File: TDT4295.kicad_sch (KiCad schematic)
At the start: 0 parts

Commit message: MCU SD-card merge
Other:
- added sheet MCU (MCU.kicad_sch)
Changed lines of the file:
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@@
+	)
+	(sheet
+		(at 140.97 15.24)
+		(size 48.26 38.1)
+		(exclude_from_sim no)
+		(in_bom yes)
+		(on_board yes)
+		(dnp no)
+		(fields_autoplaced yes)
+		(stroke
+			(width 0.1524)
+			(type solid)
+		)
+		(fill
+			(color 0 0 0 0.0000)
+		)
+		(property "Sheetname" "MCU"
+			(at 140.97 14.5284 0)
+			(effects
+				(font
+					(size 1.27 1.27)
+				)
+				(justify left bottom)
+			)
+		)
+		(property "Sheetfile" "MCU.kicad_sch"
+			(at 140.97 53.9246 0)
+			(effects
+				(font
+					(size 1.27 1.27)
+				)
+				(justify left top)
+			)
+		)
+		(instances
+			(project "TDT4295"
+				(path "/071102f3-276b-4b6b-8738-8c534a30b197"
+					(page "4")
+				)
+			)
+		)
 	)
 	(sheet

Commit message: link fpga
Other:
- added sheet FPGA (FPGA.kicad_sch)
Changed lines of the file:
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@@
+	)
+	(sheet
+		(at 19.05 45.72)
+		(size 38.735 33.02)
+		(exclude_from_sim no)
+		(in_bom yes)
+		(on_board yes)
+		(dnp no)
+		(fields_autoplaced yes)
+		(stroke
+			(width 0.1524)
+			(type solid)
+		)
+		(fill
+			(color 0 0 0 0.0000)
+		)
+		(property "Sheetname" "FPGA"
+			(at 19.05 45.0084 0)
+			(effects
+				(font
+					(size 1.27 1.27)
+				)
+				(justify left bottom)
+			)
+		)
+		(property "Sheetfile" "FPGA.kicad_sch"
+			(at 19.05 79.3246 0)
+			(effects
+				(font
+					(size 1.27 1.27)
+				)
+				(justify left top)
+			)
+		)
+		(instances
+			(project "TDT4295"
+				(path "/071102f3-276b-4b6b-8738-8c534a30b197"
+					(page "6")
+				)
+			)
+		)
 	)
 	(sheet

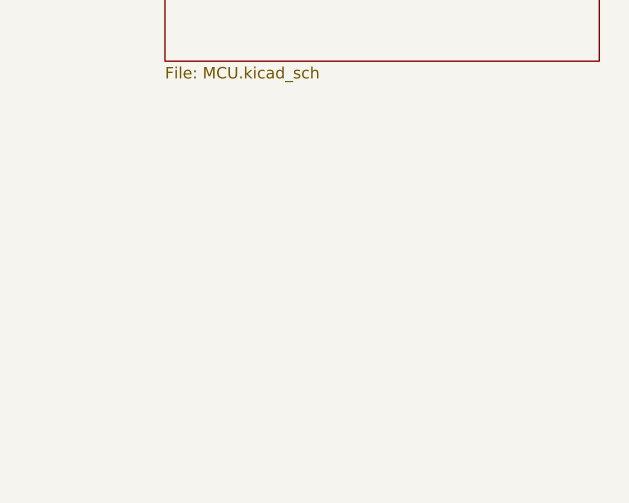
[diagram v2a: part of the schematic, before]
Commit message: schematic for stm32u545
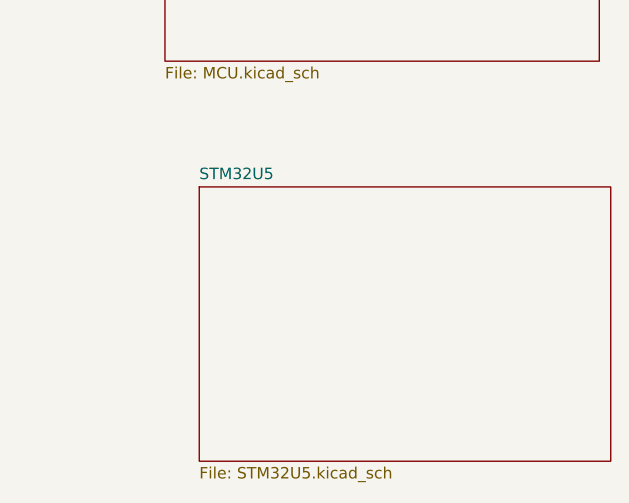
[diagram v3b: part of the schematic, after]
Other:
- added sheet STM32U5 (STM32U5.kicad_sch)
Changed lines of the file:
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@@
+	)
+	(sheet
+		(at 144.78 67.31)
+		(size 45.72 30.48)
+		(exclude_from_sim no)
+		(in_bom yes)
+		(on_board yes)
+		(dnp no)
+		(fields_autoplaced yes)
+		(stroke
+			(width 0.1524)
+			(type solid)
+		)
+		(fill
+			(color 0 0 0 0.0000)
+		)
+		(property "Sheetname" "STM32U5"
+			(at 144.78 66.5984 0)
+			(effects
+				(font
+					(size 1.27 1.27)
+				)
+				(justify left bottom)
+			)
+		)
+		(property "Sheetfile" "STM32U5.kicad_sch"
+			(at 144.78 98.3746 0)
+			(effects
+				(font
+					(size 1.27 1.27)
+				)
+				(justify left top)
+			)
+		)
+		(instances
+			(project "TDT4295"
+				(path "/071102f3-276b-4b6b-8738-8c534a30b197"
+					(page "7")
+				)
+			)
+		)
 	)
 	(sheet

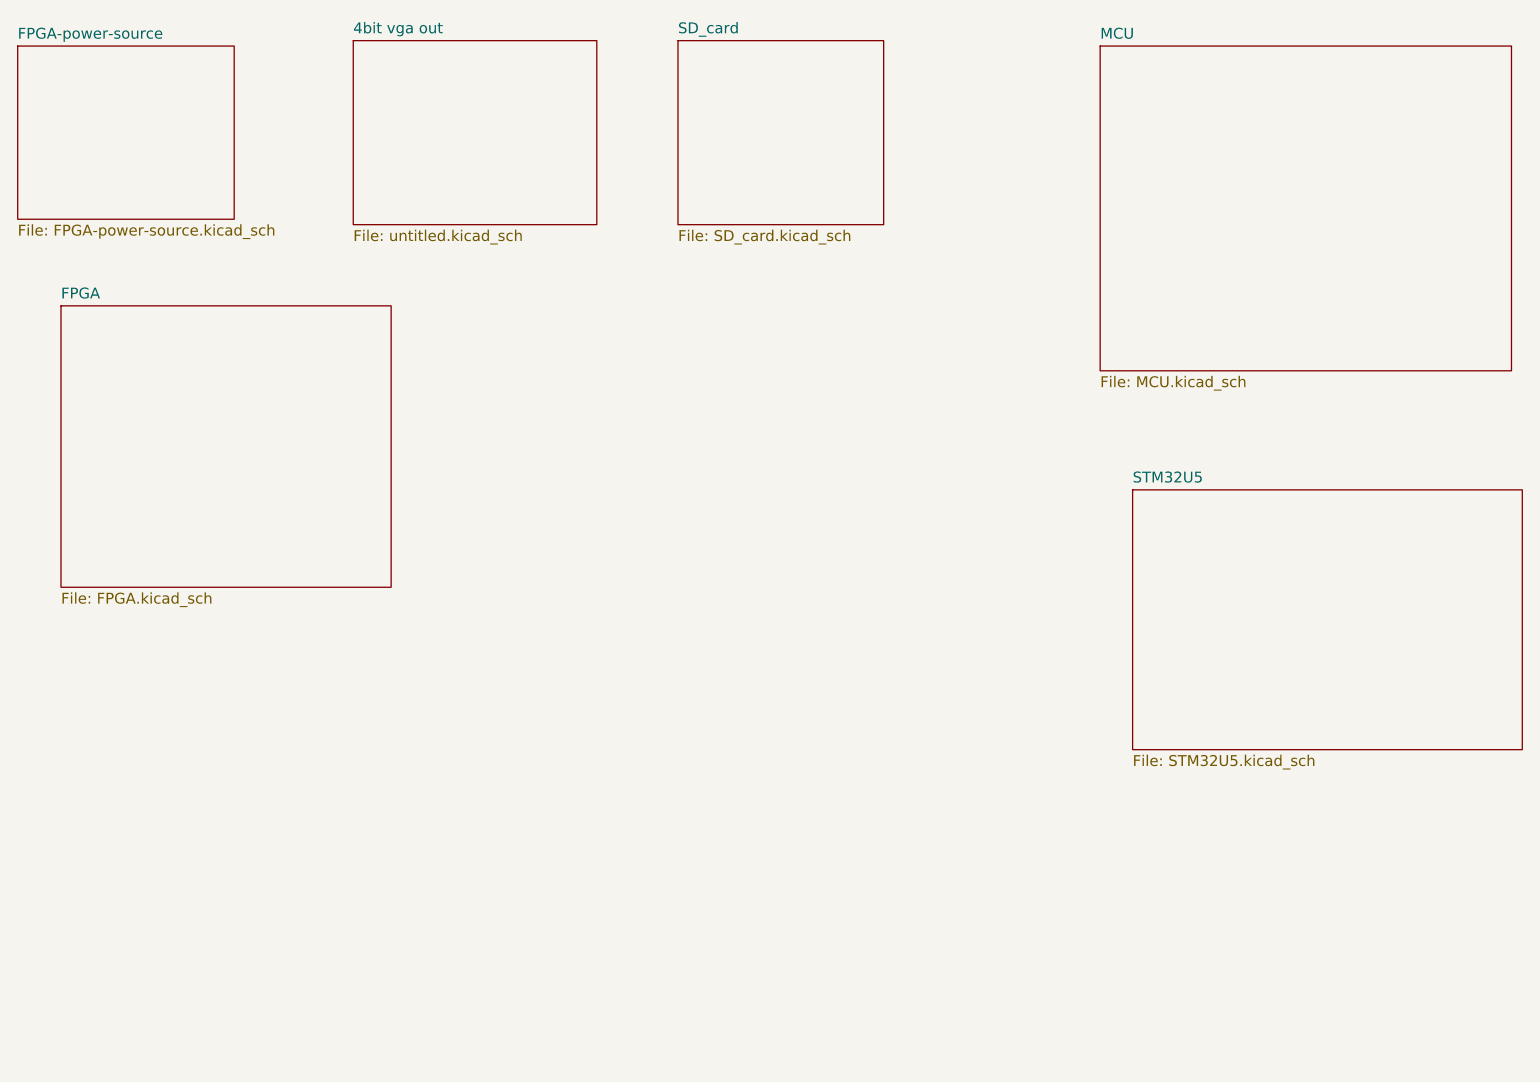
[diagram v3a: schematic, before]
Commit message: Added controllers
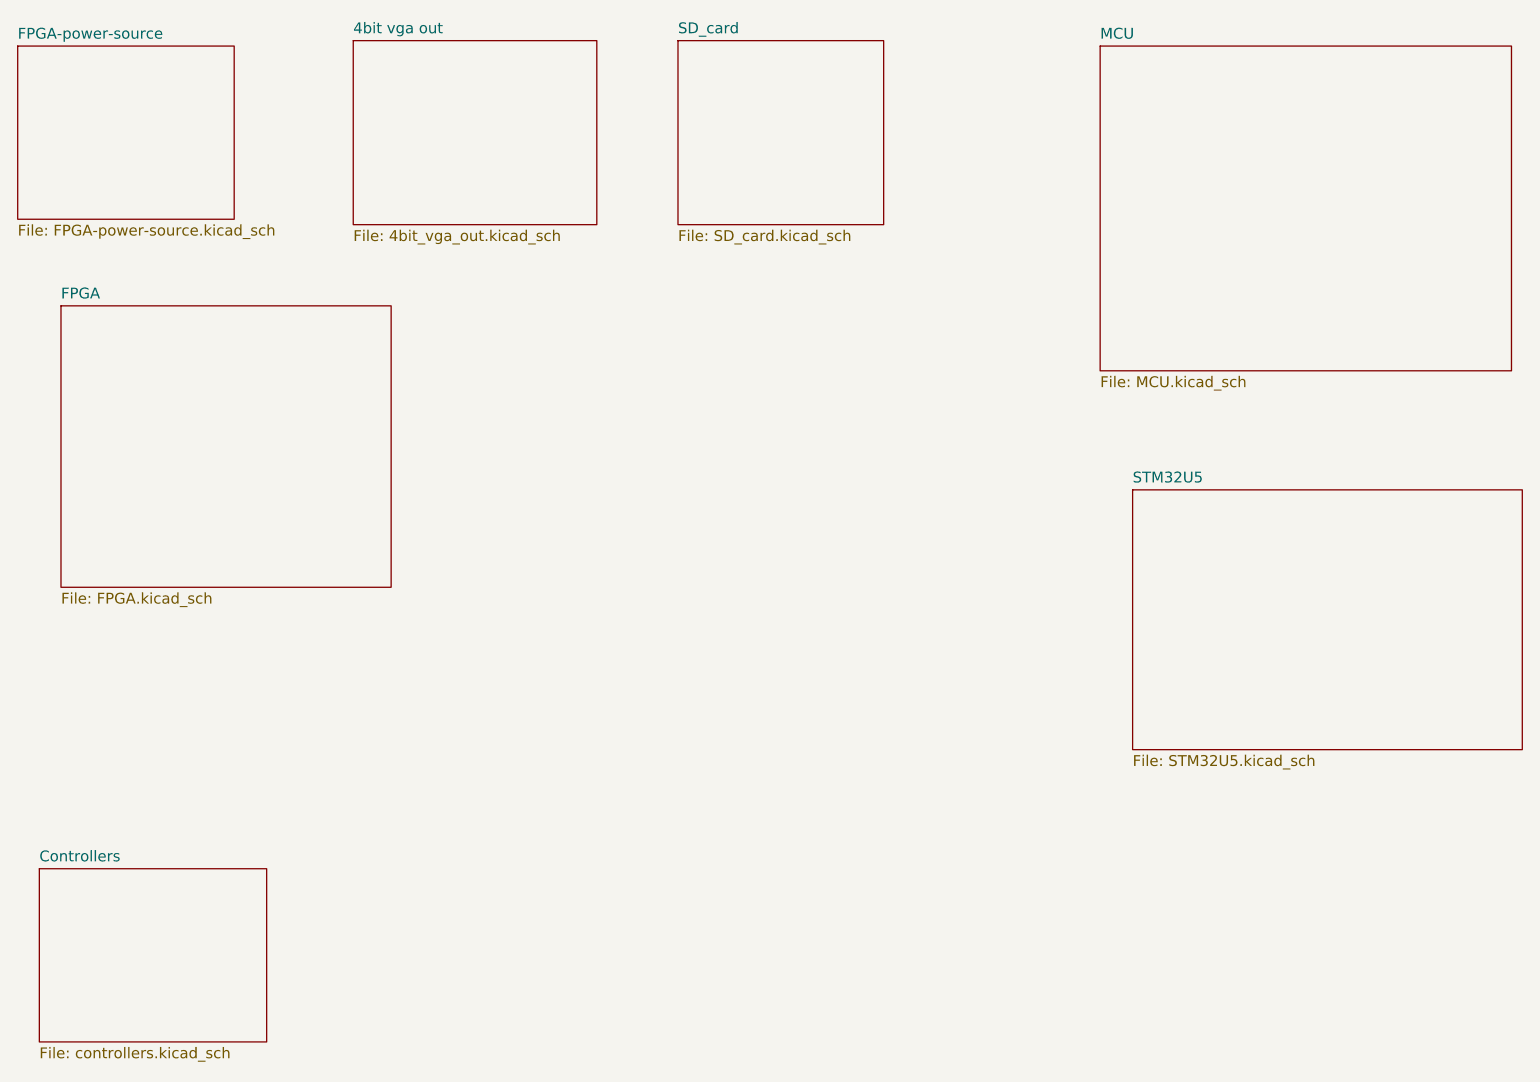
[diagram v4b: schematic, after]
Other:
- added sheet Controllers (controllers.kicad_sch)
- sheet 4bit vga out: file untitled.kicad_sch -> 4bit_vga_out.kicad_sch
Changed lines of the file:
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@@
 			)
 		)
-		(property "Sheetfile" "untitled.kicad_sch"
+		(property "Sheetfile" "4bit_vga_out.kicad_sch"
 			(at 53.34 36.7796 0)
 			(effects
@@
 				)
 			)
+		)
+	)
+	(sheet
+		(at 16.51 111.76)
+		(size 26.67 20.32)
+		(exclude_from_sim no)
+		(in_bom yes)
+		(on_board yes)
+		(dnp no)
+		(fields_autoplaced yes)
+		(stroke
+			(width 0.1524)
+			(type solid)
+		)
+		(fill
+			(color 0 0 0 0.0000)
+		)
+		(property "Sheetname" "Controllers"
+			(at 16.51 111.0484 0)
+			(effects
+				(font
+					(size 1.27 1.27)
+				)
+				(justify left bottom)
+			)
+		)
+		(property "Sheetfile" "controllers.kicad_sch"
+			(at 16.51 132.6646 0)
+			(effects
+				(font
+					(size 1.27 1.27)
+				)
+				(justify left top)
+			)
+		)
+		(instances
+			(project "TDT4295"
+				(path "/071102f3-276b-4b6b-8738-8c534a30b197"
+					(page "8")
+				)
+			)

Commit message: Added display connector
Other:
- added sheet Display (display.kicad_sch)
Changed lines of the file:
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@@
+		)
+	)
+	(sheet
+		(at 102.87 76.2)
+		(size 30.48 20.32)
+		(exclude_from_sim no)
+		(in_bom yes)
+		(on_board yes)
+		(dnp no)
+		(fields_autoplaced yes)
+		(stroke
+			(width 0.1524)
+			(type solid)
+		)
+		(fill
+			(color 0 0 0 0.0000)
+		)
+		(property "Sheetname" "Display"
+			(at 102.87 75.4884 0)
+			(effects
+				(font
+					(size 1.27 1.27)
+				)
+				(justify left bottom)
+			)
+		)
+		(property "Sheetfile" "display.kicad_sch"
+			(at 102.87 97.1046 0)
+			(effects
+				(font
+					(size 1.27 1.27)
+				)
+				(justify left top)
+			)
+		)
+		(instances
+			(project "TDT4295"
+				(path "/071102f3-276b-4b6b-8738-8c534a30b197"
+					(page "9")
+				)
+			)
 		)
 	)
